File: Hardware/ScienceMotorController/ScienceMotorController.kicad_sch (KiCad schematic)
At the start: 197 parts, among them J1 RJ45_LED_Shielded, Q1 SI4156DY, Q10 AO3401A, Q11 SI4156DY, Q12 SI4156DY, Q13 SI4156DY, Q14 SI4156DY, Q15 SI4156DY, Q16 SI4156DY, Q17 SI4156DY, Q18 SI4156DY, Q2 SI4156DY, Q3 SI4156DY, Q4 SI4156DY, Q5 SI4156DY, Q6 SI4156DY, Q7 SI4156DY, Q8 SI4156DY, Q9 BSS138, SW1 SW_Push, SW11 SW_DPDT_x2, SW2 SW_Push, SW3 SW_Push, SW4 SW_Push, SW5 SW_Push, SW6 SW_Push, SW7 SW_Push, SW8 SW_Push, SW9 SW_Push, U1 74LVC2G04, U10 IRS2005S, U11 IRS2005S, U12 Teensy4.1_DEV-16771, U13 IRS2005S, U14 IRS2005S, U2 74LVC2G04, U3 IRS2005S, U4 IRS2005S, U5 TSR_1-2450, U6 IRS2005S, U7 IRS2005S, U8 74LVC2G04, U9 74LVC2G04

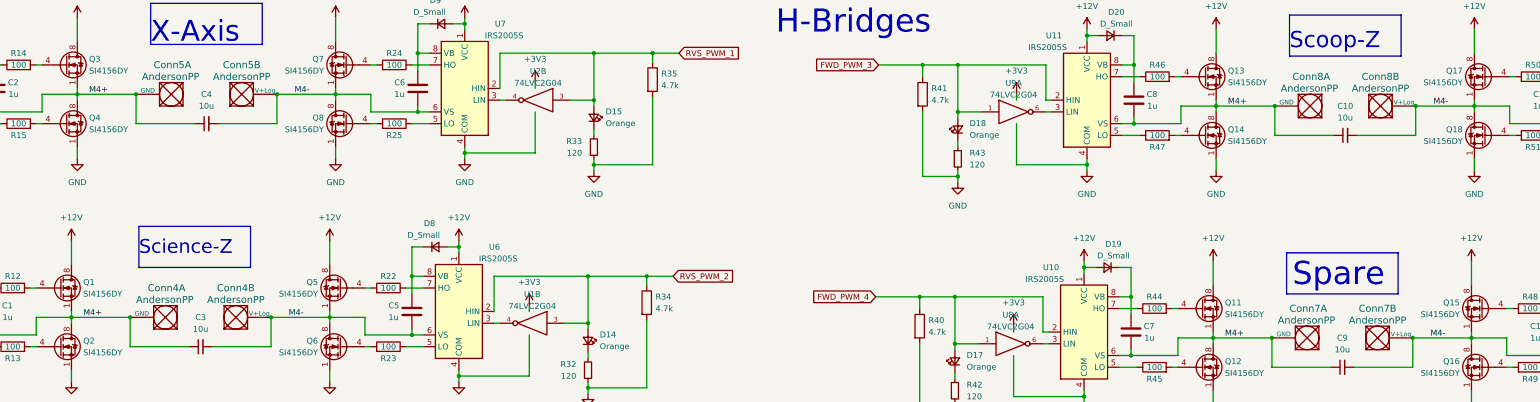
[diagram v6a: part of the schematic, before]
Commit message: Power anderson footprint changed and more GND vias
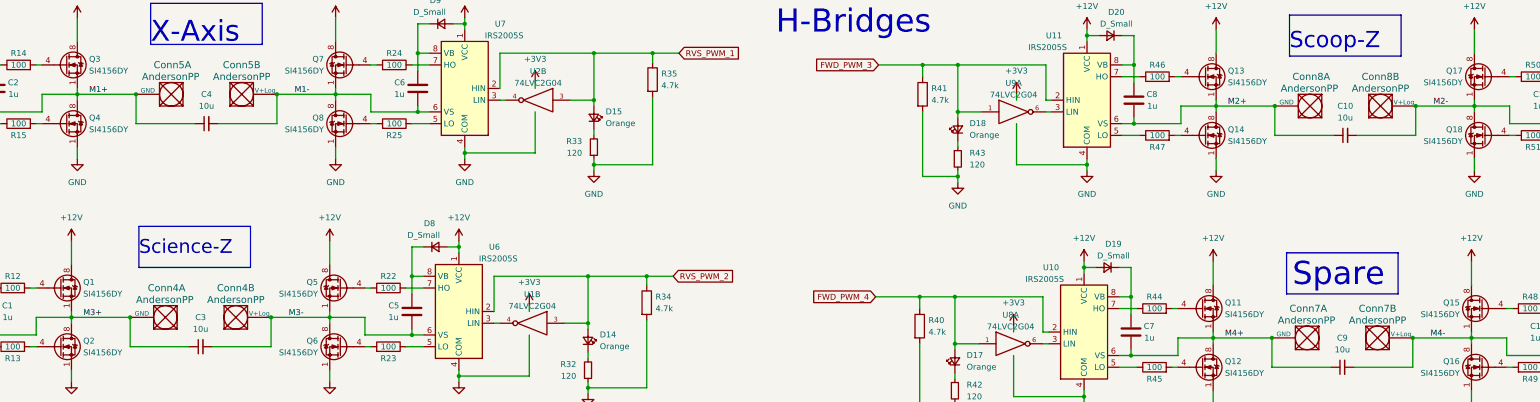
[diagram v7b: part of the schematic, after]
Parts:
- Conn1, Conn2, Conn3: footprint MRDT_Connectors:Square_Anderson_2_H_Side_By_Side -> MRDT_Connectors:Square_Anderson_2_H_Stacked_PV
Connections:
- net M4+: no longer C1.2, C10.1, C2.2, C3.1, C4.1, C8.2, Conn4.1 (GND), Conn5.1 (GND), Conn8.1 (GND), Q1.1 (S), Q1.2 (S), Q1.3 (S), Q13.1 (S), Q13.2 (S), Q13.3 (S), Q14.5 (D), Q14.6 (D), Q14.7 (D), Q14.8 (D), Q2.5 (D), Q2.6 (D), Q2.7 (D), Q2.8 (D), Q3.1 (S), Q3.2 (S), Q3.3 (S), Q4.5 (D), Q4.6 (D), Q4.7 (D), Q4.8 (D), U11.6 (VS), U3.6 (VS), U4.6 (VS)
- net M4-: no longer C10.2, C12.2, C3.2, C4.2, C5.2, C6.2, Conn4.2 (V+Log), Conn5.2 (V+Log), Conn8.2 (V+Log), Q17.1 (S), Q17.2 (S), Q17.3 (S), Q18.5 (D), Q18.6 (D), Q18.7 (D), Q18.8 (D), Q5.1 (S), Q5.2 (S), Q5.3 (S), Q6.5 (D), Q6.6 (D), Q6.7 (D), Q6.8 (D), Q7.1 (S), Q7.2 (S), Q7.3 (S), Q8.5 (D), Q8.6 (D), Q8.7 (D), Q8.8 (D), U14.6 (VS), U6.6 (VS), U7.6 (VS)
- new net M1+: C2.2, C4.1, Conn5.1 (GND), Q3.1 (S), Q3.2 (S), Q3.3 (S), Q4.5 (D), Q4.6 (D), Q4.7 (D), Q4.8 (D), U4.6 (VS)
- new net M1-: C4.2, C6.2, Conn5.2 (V+Log), Q7.1 (S), Q7.2 (S), Q7.3 (S), Q8.5 (D), Q8.6 (D), Q8.7 (D), Q8.8 (D), U7.6 (VS)
- new net M2+: C10.1, C8.2, Conn8.1 (GND), Q13.1 (S), Q13.2 (S), Q13.3 (S), Q14.5 (D), Q14.6 (D), Q14.7 (D), Q14.8 (D), U11.6 (VS)
- new net M2-: C10.2, C12.2, Conn8.2 (V+Log), Q17.1 (S), Q17.2 (S), Q17.3 (S), Q18.5 (D), Q18.6 (D), Q18.7 (D), Q18.8 (D), U14.6 (VS)
- new net M3+: C1.2, C3.1, Conn4.1 (GND), Q1.1 (S), Q1.2 (S), Q1.3 (S), Q2.5 (D), Q2.6 (D), Q2.7 (D), Q2.8 (D), U3.6 (VS)
- new net M3-: C3.2, C5.2, Conn4.2 (V+Log), Q5.1 (S), Q5.2 (S), Q5.3 (S), Q6.5 (D), Q6.6 (D), Q6.7 (D), Q6.8 (D), U6.6 (VS)
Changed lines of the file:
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@@
     (effects (font (size 1.27 1.27)) (justify left bottom))
   )
-  (label "M4-" (at 154.94 105.41 0)
+  (label "M3-" (at 154.94 105.41 0)
     (effects (font (size 1.27 1.27)) (justify left bottom))
   )
@@
     (effects (font (size 1.27 1.27)) (justify left bottom))
   )
-  (label "M4+" (at 111.76 57.15 0)
+  (label "M1+" (at 111.76 57.15 0)
     (effects (font (size 1.27 1.27)) (justify left bottom))
   )
@@
     (effects (font (size 1.27 1.27)) (justify left bottom))
   )
-  (label "M4+" (at 358.14 59.69 0)
+  (label "M2+" (at 358.14 59.69 0)
     (effects (font (size 1.27 1.27)) (justify left bottom))
   )
-  (label "M4-" (at 402.59 59.69 0)
+  (label "M2-" (at 402.59 59.69 0)
     (effects (font (size 1.27 1.27)) (justify left bottom))
   )
@@
     (effects (font (size 1.27 1.27)) (justify left bottom))
   )
-  (label "M4+" (at 110.49 105.41 0)
+  (label "M3+" (at 110.49 105.41 0)
     (effects (font (size 1.27 1.27)) (justify left bottom))
   )
-  (label "M4-" (at 156.21 57.15 0)
+  (label "M1-" (at 156.21 57.15 0)
     (effects (font (size 1.27 1.27)) (justify left bottom))
   )
@@
       (effects (font (size 1.524 1.524)) (justify right))
     )
-    (property "Footprint" "MRDT_Connectors:Square_Anderson_2_H_Side_By_Side" (id 2) (at 96.774 302.26 0)
+    (property "Footprint" "MRDT_Connectors:Square_Anderson_2_H_Stacked_PV" (id 2) (at 96.774 302.26 0)
       (effects (font (size 1.524 1.524)) hide)
     )
@@
       (effects (font (size 1.524 1.524)))
     )
-    (property "Footprint" "MRDT_Connectors:Square_Anderson_2_H_Side_By_Side" (id 2) (at 29.972 339.344 0)
+    (property "Footprint" "MRDT_Connectors:Square_Anderson_2_H_Stacked_PV" (id 2) (at 29.972 339.344 0)
       (effects (font (size 1.524 1.524)) hide)
     )
@@
       (effects (font (size 1.524 1.524)) (justify right))
     )
-    (property "Footprint" "MRDT_Connectors:Square_Anderson_2_H_Side_By_Side" (id 2) (at 130.048 296.164 0)
+    (property "Footprint" "MRDT_Connectors:Square_Anderson_2_H_Stacked_PV" (id 2) (at 130.048 296.164 0)
       (effects (font (size 1.524 1.524)) hide)
     )
@@
       (effects (font (size 1.524 1.524)) (justify right))
     )
-    (property "Footprint" "MRDT_Connectors:Square_Anderson_2_H_Side_By_Side" (id 2) (at 130.048 302.514 0)
+    (property "Footprint" "MRDT_Connectors:Square_Anderson_2_H_Stacked_PV" (id 2) (at 130.048 302.514 0)
       (effects (font (size 1.524 1.524)) hide)
     )
@@
       (effects (font (size 1.524 1.524)))
     )
-    (property "Footprint" "MRDT_Connectors:Square_Anderson_2_H_Side_By_Side" (id 2) (at 29.972 329.184 0)
+    (property "Footprint" "MRDT_Connectors:Square_Anderson_2_H_Stacked_PV" (id 2) (at 29.972 329.184 0)
       (effects (font (size 1.524 1.524)) hide)
     )
@@
       (effects (font (size 1.524 1.524)) (justify right))
     )
-    (property "Footprint" "MRDT_Connectors:Square_Anderson_2_H_Side_By_Side" (id 2) (at 96.774 295.91 0)
+    (property "Footprint" "MRDT_Connectors:Square_Anderson_2_H_Stacked_PV" (id 2) (at 96.774 295.91 0)
       (effects (font (size 1.524 1.524)) hide)
     )
@@
     )
     (path "/306b25a5-298c-4dea-93a1-3a59ea7e061c"
-      (reference "Conn1") (unit 1) (value "AndersonPP") (footprint "MRDT_Connectors:Square_Anderson_2_H_Side_By_Side")
+      (reference "Conn1") (unit 1) (value "AndersonPP") (footprint "MRDT_Connectors:Square_Anderson_2_H_Stacked_PV")
     )
     (path "/97bf378c-365e-439d-b3f6-619cb43cad33"
-      (reference "Conn1") (unit 2) (value "AndersonPP") (footprint "MRDT_Connectors:Square_Anderson_2_H_Side_By_Side")
+      (reference "Conn1") (unit 2) (value "AndersonPP") (footprint "MRDT_Connectors:Square_Anderson_2_H_Stacked_PV")
     )
     (path "/dda92378-fdc5-4464-a82a-89afd2a6b2ce"
-      (reference "Conn2") (unit 1) (value "Output1") (footprint "MRDT_Connectors:Square_Anderson_2_H_Side_By_Side")
+      (reference "Conn2") (unit 1) (value "Output1") (footprint "MRDT_Connectors:Square_Anderson_2_H_Stacked_PV")
     )
     (path "/1d51c736-ab33-4442-88c2-b9ab66235ee4"
-      (reference "Conn2") (unit 2) (value "Output1") (footprint "MRDT_Connectors:Square_Anderson_2_H_Side_By_Side")
+      (reference "Conn2") (unit 2) (value "Output1") (footprint "MRDT_Connectors:Square_Anderson_2_H_Stacked_PV")
     )
     (path "/3183b2c9-8229-49d0-a050-755a27766c98"
-      (reference "Conn3") (unit 1) (value "Output2") (footprint "MRDT_Connectors:Square_Anderson_2_H_Side_By_Side")
+      (reference "Conn3") (unit 1) (value "Output2") (footprint "MRDT_Connectors:Square_Anderson_2_H_Stacked_PV")
     )
     (path "/60557573-9f6e-4cb2-9497-0b8332d3ecf4"
-      (reference "Conn3") (unit 2) (value "Output2") (footprint "MRDT_Connectors:Square_Anderson_2_H_Side_By_Side")
+      (reference "Conn3") (unit 2) (value "Output2") (footprint "MRDT_Connectors:Square_Anderson_2_H_Stacked_PV")
     )
     (path "/05c82a10-45ea-46b1-8378-4aa3909da2e4"

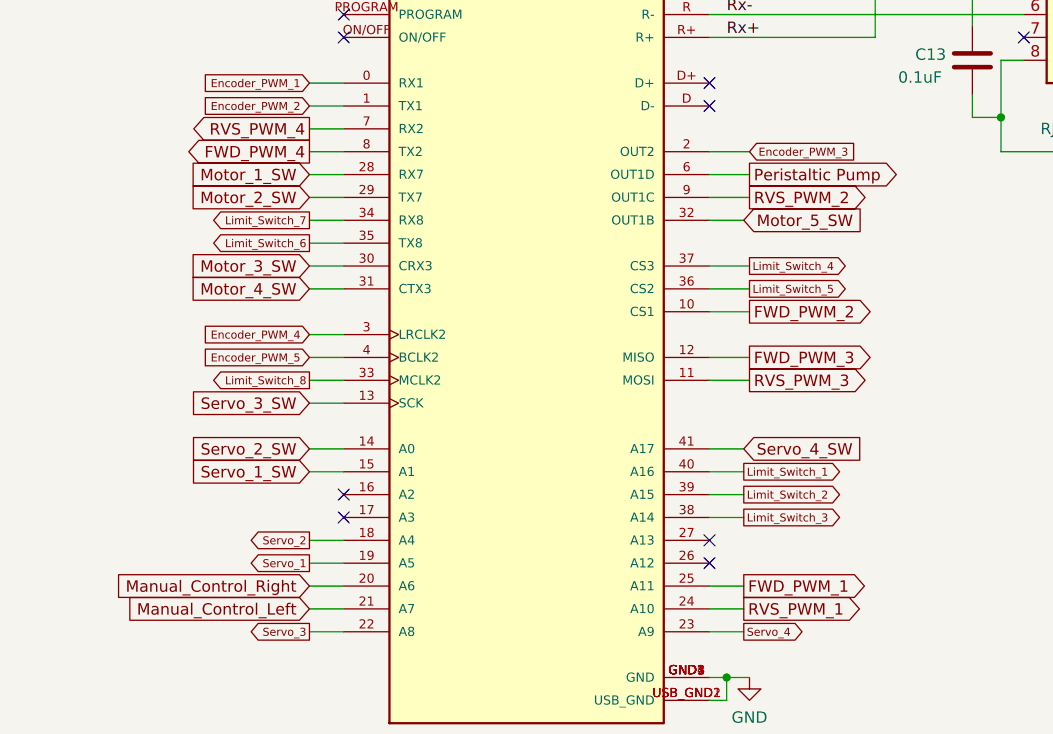
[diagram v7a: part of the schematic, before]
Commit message: Board has been shrunk.
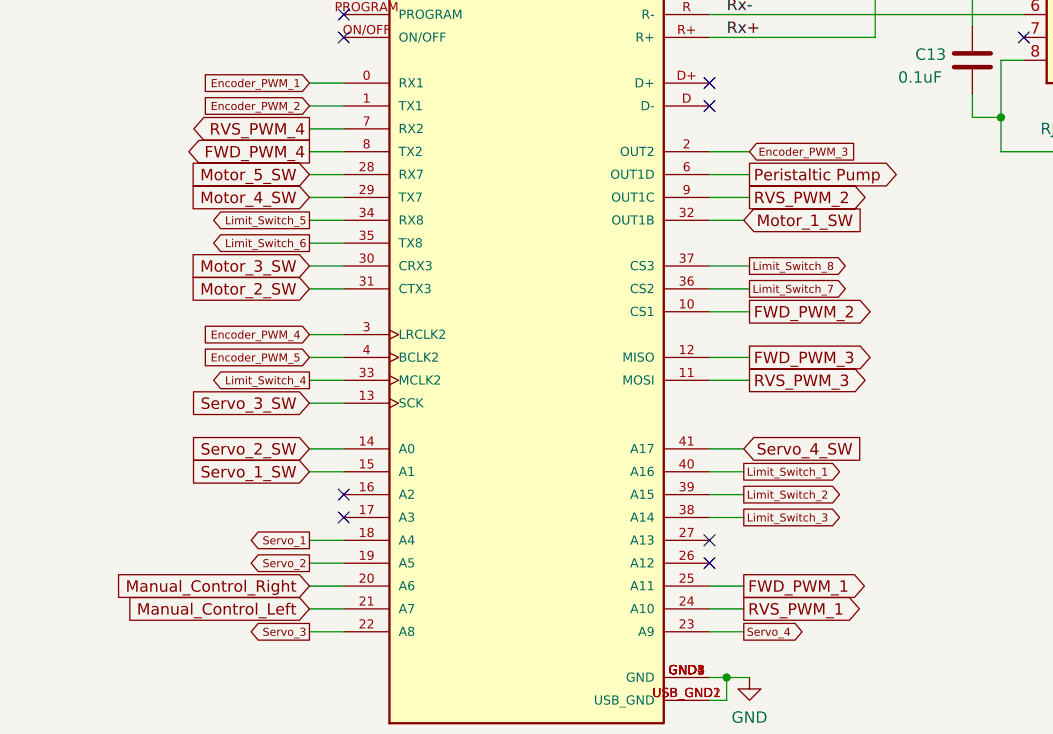
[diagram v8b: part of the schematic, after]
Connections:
- net Limit_Switch_4: now also U12.33 (MCLK2); no longer U12.37 (CS3)
- net Limit_Switch_5: now also U12.34 (RX8); no longer U12.36 (CS2)
- net Limit_Switch_7: now also U12.36 (CS2); no longer U12.34 (RX8)
- net Limit_Switch_8: now also U12.37 (CS3); no longer U12.33 (MCLK2)
- net Motor_1_SW: now also U12.32 (OUT1B); no longer U12.28 (RX7)
- net Motor_2_SW: now also U12.31 (CTX3); no longer U12.29 (TX7)
- net Motor_4_SW: now also U12.29 (TX7); no longer U12.31 (CTX3)
- net Motor_5_SW: now also U12.28 (RX7); no longer U12.32 (OUT1B)
- net Servo_1: now also U12.18 (A4); no longer U12.19 (A5)
- net Servo_2: now also U12.19 (A5); no longer U12.18 (A4)
